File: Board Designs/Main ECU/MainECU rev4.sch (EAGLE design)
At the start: 145 parts, among them X1 CONNECTOR-37, X2 CONNECTOR-4AUTOSPORT, X3 CONNECTOR-4NANO-FIT-VERTICAL-4, X4 CONNECTOR-4NANO-FIT-VERTICAL-4

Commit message: Rename Main ECU rev1b -> rev3, rev3 -> rev4
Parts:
- removed AC1_FILTR, AC2_FILTR: 510, HyTechDevices:RESISTOR0805-RES
- removed BRAKE_LIGHT_SSR, FAN_SSR1, FAN_SSR2, INVERTER_SSR, PUMP_SSR: CPC1002N, HyTechDevices:CPC1002N
- removed BR_FILTR: 100, HyTechDevices:RESISTOR0805-RES
- removed C13: .1uF, HyTechDevices:CAP0805
- removed LED12, LED13, LED16, LED4: Red, HyTechDevices:LED-0805
- removed R25: 330, HyTechDevices:RESISTOR0805-RES
- removed REG2: 5V, HyTechDevices:OKI-78SR
- removed U$20, U$21, U$22: JUMPER, HyTechDevices:JUMPER
- added C14, C17: 47pF, HyTechDevices:CAP0805
- added C15, C16, C18, C19, C21: .1uF, HyTechDevices:CAP0805
- added C20: .22uF, HyTechDevices:CAP0805
- added CAN_TRANSCEIVER2: MCP2551, HyTechDevices:MCP2551
- added Q1, Q11, Q2, Q3, Q4, Q5, Q6, Q7, Q8, Q9: MMBT3904LT3G, HyTechDevices:BJT_NPNSOT
- added Q10: (no value), HyTechDevices:BJT_NPNSOT
- added R46: 120, HyTechDevices:RESISTOR0805-RES
- added R47, R50: 2.2k, HyTechDevices:RESISTOR0805-RES
- added R48: 10k, HyTechDevices:RESISTOR0805-RES
- added R49: 1.2k, HyTechDevices:RESISTOR0805-RES
- added REG3: 5V, HyTechDevices:OKI-78SR
- added U$27, U$28: (no value), HyTechDevices:MAX7480
- C11: value .22uF -> (none)
- C12: value 2.2µ -> .1uF
- C3: value 22µ -> 47pF
- C4: value 22µ -> .1uF
- D7, D8, D9: value DIODE0805 -> MMBZ5246BLT1G; device HyTechDevices:DIODE0805 -> HyTechDevices:DIODE_ZENER
- R10: value 43 -> 2.2k
- R16: value 43 -> 100
- R24, R27, R28: value 33 -> 10k
- R35, R36, R38, R39, R40, R41, R42: value 270 -> 2.2k
- R37: value 270 -> 0
- R44: value 0 -> 2.2k
- U$11, U$12: value TLP291-4 -> JUMPER; device HyTechDevices:TLP291-4 -> HyTechDevices:JUMPER
- U$15: value SN74LV1T34 -> BJT_PNPSOT; device HyTechDevices:SN74LV1T34 -> HyTechDevices:BJT_PNPSOT
- U$16: value JUMPER -> CR-2450/G1AN; device HyTechDevices:JUMPER -> HyTechDevices:CR-2450/G1AN
- U$19: value JUMPER -> MC34152; device HyTechDevices:JUMPER -> HyTechDevices:MC34152
- U$26: value CR-2450/G1AN -> (none); device HyTechDevices:CR-2450/G1AN -> HyTechDevices:MAX7480
- U$4, U$6, U$7: value G5LE -> N-CHANNEL_MOSFET_FQP30N06L; device HyTechDevices:G5LE -> HyTechDevices:N-CHANNEL_MOSFET_HOR_HOLE
- U$5: value CPC1002N -> MC34152; device HyTechDevices:CPC1002N -> HyTechDevices:MC34152
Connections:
- removed net DASH_CTRL5: R39.1, U$17.GPA4
- removed net DASH_CTRL6: R40.1, U$13.P$2, U$17.GPA5
- removed net DASH_CTRL7: R41.1, U$14.P$2, U$17.GPA6
- removed net DASH_CTRL8: R42.1, U$15.2, U$17.GPA7, U$19.P$2
- removed net N$20: D8.C, FAN_SSR1.DC-, U$7.COIL-
- removed net N$39: FAN_SSR2.CONTROL-, LED16.A
- removed net N$43: D10.C, R26.1, SOFTWARE_SHUTOFF.COIL-, U$5.DC-
- removed net N$44: R25.2, U$5.CONTROL-
- removed net RELAY_CTRL1: PUMP_SSR.CONTROL+, U$1.A9
- removed net RELAY_CTRL2: FAN_SSR1.CONTROL+, U$1.D2
- removed net RELAY_CTRL3: FAN_SSR2.CONTROL+, U$1.A8
- new net DASH_CTRL5_IN: U$12.P$2, U$17.GPA4
- new net DASH_CTRL5_OUT: R40.1, U$17.GPB4
- new net DASH_CTRL6_IN: U$11.P$2, U$17.GPA5
- new net DASH_CTRL6_OUT: R41.1, U$17.GPB5
- new net DASH_CTRL7_IN: U$13.P$2, U$17.GPA6
- new net DASH_CTRL7_OUT: R42.1, U$17.GPB6
- new net DASH_CTRL8_IN: U$14.P$2, U$17.GPA7
- new net DASH_CTRL8_OUT: R44.1, U$17.GPB7
- new net FAN1CONTROL: U$1.A8, U$5.IN_A
- new net FAN1DRIVE: D8.C, R24.2, U$5.OUT_A, U$7.G
- new net FAN2CONTROL: U$1.A9, U$5.IN_B
- new net FAN2DRIVE: D7.C, R28.2, U$4.G, U$5.OUT_B
- new net N$66: D4.A, Q9.COLLECTOR, U$8.COIL-
- new net PUMPCONTROL: U$1.A6, U$19.IN_A
- new net PUMPDRIVE: D9.C, R27.2, U$19.OUT_A, U$6.G
- new net TELEMETRY_CANH: CAN_TRANSCEIVER2.7, R46.2, X4-4.S
- new net TELEMETRY_CANL: CAN_TRANSCEIVER2.6, R46.1, X4-3.S
- net +12V: now also C20.2, D10.C, D4.C, R48.1, REG3.IN, SOFTWARE_SHUTOFF.COIL-, U$15.E, U$19.VCC, U$5.VCC, U$8.COIL+; no longer BRAKE_LIGHT_SSR.DC+, C11.2, FAN_SSR1.DC+, FAN_SSR2.DC+, INVERTER_SSR.DC+, PUMP_SSR.DC+, REG2.IN, U$11.C3, U$11.C4, U$12.C1, U$12.C2, U$12.C3, U$12.C4, U$16.P$1, U$21.P$1, U$5.DC+
- net +5V: now also C11.2, C15.1, C18.1, C4.1, U$26.!SHDN, U$26.VDD, U$27.!SHDN, U$27.VDD, U$28.!SHDN, U$28.VDD; no longer U$15.5, U$20.P$1, U$22.P$1
- net BRAKE_LIGHT: now also U$15.C; no longer BRAKE_LIGHT_SSR.DC-
- net CANH: no longer X4-4.S
- net CANL: no longer X4-3.S
- net DASH_CTRL1: now also U$17.GPB0; no longer U$17.GPA0
- net DASH_CTRL10: now also U$17.GPA1; no longer U$17.GPB1
- net DASH_CTRL11: now also U$17.GPA2; no longer U$17.GPB2
- net DASH_CTRL12: now also U$17.GPA3; no longer U$17.GPB3
- net DASH_CTRL2: now also U$17.GPB1; no longer U$17.GPA1
- net DASH_CTRL3: now also R38.1, U$17.GPB2; no longer R37.1, U$17.GPA2
- net DASH_CTRL4: now also R39.1, U$17.GPB3; no longer R38.1, U$17.GPA3
- net DASH_CTRL9: now also U$17.GPA0; no longer U$17.GPB0
- net DASH_IO2: now also R37.2; no longer R44.2
- net DASH_IO3: now also Q3.COLLECTOR; no longer U$12.EM2
- net DASH_IO4: now also Q4.COLLECTOR; no longer U$12.EM1
- net DASH_IO5: now also Q5.COLLECTOR, U$12.P$1; no longer U$11.EM4
- net DASH_IO6: now also Q6.COLLECTOR, U$11.P$1; no longer U$11.EM3, U$13.P$1
- net DASH_IO7: now also Q7.COLLECTOR, U$13.P$1; no longer U$11.EM2, U$14.P$1
- net DASH_IO8: now also Q8.COLLECTOR, U$14.P$1; no longer U$11.EM1, U$15.4, U$19.P$1
- net FAN1-: now also U$7.D; no longer U$7.P
- net FAN2-: now also U$4.D; no longer U$4.P
- net GND: now also C14.2, C15.2, C16.1, C17.2, C18.2, C19.1, C20.1, C21.1, CAN_TRANSCEIVER2.2, CAN_TRANSCEIVER2.8, Q1.EMITTER, Q10.EMITTER, Q11.EMITTER, Q2.EMITTER, Q3.EMITTER, Q4.EMITTER, Q5.EMITTER, Q6.EMITTER, Q7.EMITTER, Q8.EMITTER, Q9.EMITTER, R24.1, R27.1, R28.1, REG3.GND, U$19.GND, U$25.GND, U$26.GND, U$27.GND, U$28.GND, U$5.GND; no longer C13.1, D10.A, D4.A, LED4.C, R24.2, R25.1, R27.2, R28.2, REG2.GND, SOFTWARE_SHUTOFF.COIL+, U$11.GND1, U$11.GND2, U$11.GND3, U$11.GND4, U$12.GND1, U$12.GND2, U$12.GND3, U$12.GND4, U$15.3, U$4.COIL+, U$6.COIL+, U$7.COIL+, U$8.COIL-
- net INVERTER_CTRL: now also R16.1, R47.1; no longer INVERTER_SSR.CONTROL+
- net N$17: now also Q10.COLLECTOR, R48.2, R49.1; no longer BRAKE_LIGHT_SSR.CONTROL+, R10.1
- net N$21: now also C3.1, U$27.CLK; no longer D9.C, FAN_SSR2.DC-, U$4.COIL-
- net N$23: now also U$28.IN; no longer AC2_FILTR.1
- net N$24: now also U$27.IN; no longer AC1_FILTR.1
- net N$25: now also U$26.IN; no longer BR_FILTR.1
- net N$26: now also Q11.BASE, R50.2; no longer D4.C, INVERTER_SSR.DC-, U$8.COIL+
- net N$27: now also D10.A, Q11.COLLECTOR, SOFTWARE_SHUTOFF.COIL+; no longer INVERTER_SSR.CONTROL-, R16.1
- net N$30: now also Q2.BASE, R36.2; no longer LED16.C, R24.1
- net N$36: now also C16.2, U$28.COM, U$28.OS; no longer LED13.C, R28.1
- net N$37: now also C19.2, U$26.COM, U$26.OS; no longer LED12.C, R27.1
- net N$38: now also C14.1, U$28.CLK; no longer LED12.A, PUMP_SSR.CONTROL-
- net N$4: now also C12.2, U$27.COM, U$27.OS; no longer D7.C, PUMP_SSR.DC-, U$6.COIL-
- net N$41: now also C17.1, U$26.CLK; no longer U$2.3.3V_2, U$26.+
- net N$42: now also Q2.COLLECTOR, R37.1; no longer FAN_SSR1.CONTROL-, LED13.A
- net N$51: now also Q1.BASE; no longer U$12.VCC4
- net N$52: now also Q3.BASE, R38.2; no longer R36.2, U$12.VCC3
- net N$53: now also Q4.BASE, R39.2; no longer R37.2, U$12.VCC2
- net N$54: now also Q5.BASE, R40.2; no longer R38.2, U$12.VCC1
- net N$55: now also Q6.BASE, R41.2; no longer R39.2, U$11.VCC4
- net N$56: now also Q7.BASE, R42.2; no longer R40.2, U$11.VCC3
- net N$57: now also Q8.BASE, R44.2; no longer R41.2, U$11.VCC2
- net N$58: now also R49.2, U$15.B; no longer R42.2, U$11.VCC1
- net N$59: now also Q1.COLLECTOR; no longer U$12.EM4
- net N$60: now also U$16.+, U$2.3.3V_2; no longer R44.1, U$12.EM3
- net N$61: now also U$16.-, U$2.GND_2; no longer U$11.C1, U$16.P$2, U$20.P$2
- net N$62: now also CAN_TRANSCEIVER2.4, U$2.A15; no longer U$11.C2, U$21.P$2, U$22.P$2
- net N$64: now also CAN_TRANSCEIVER2.1, U$2.A14; no longer U$2.GND_2, U$26.-
- net N$65: now also Q9.BASE, R47.2; no longer U$25.GND
- net N$7: now also Q10.BASE, R10.1; no longer BRAKE_LIGHT_SSR.CONTROL-, LED4.A
- net PUMP1-: now also U$6.D; no longer U$6.P
- net READ_ACCEL1: now also U$27.OUT; no longer AC1_FILTR.2, C4.1
- net READ_ACCEL2: now also U$28.OUT; no longer AC2_FILTR.2, C3.1
- net READ_BRAKE: now also U$26.OUT; no longer BR_FILTR.2, C12.2
- net SOFTWARE_SHUTDOWN: now also R26.1, R50.1; no longer U$5.CONTROL+
- net TELEMETRY5V: now also C21.2, CAN_TRANSCEIVER2.3, REG3.OUT; no longer C13.2, REG2.OUT
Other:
- note added: "47pF for ~10Hz filter (11.3Hz)"
- note added: "Check Values, Switching V is 5V"
- note added: "Dash 5, 6, 7, 8 Can be inputs or outputs For input, solder jumper. For output, solder transistor and resistor."
- note added: "Pullup/down resistors to detect open circuit. Install only one per signal on ACCEL1 and ACCEL2."
- note removed: "Relays"
- note removed: "Use these jumpers or SN74LV1T34 only when optocoupler resistors are removed!"
- note removed: "Use these jumpers to select DASH_IO{7,8} output voltage"
- note removed: "⇩ Pullup/down resistors to detect open circuit. Install only one per signal on ACCEL1 and ACCEL2."
- moved on the sheet: 5ABOARDFUSE, 5AFUSE, 5ASHUTDOWNFUSE, ACC1_PD, ACC1_PU, ACC2_PD, ACC2_PU, ADXL345_BREAKOUT, BMS_LATCH_SSR, BMS_SSR, BOARD_TEMP, C1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

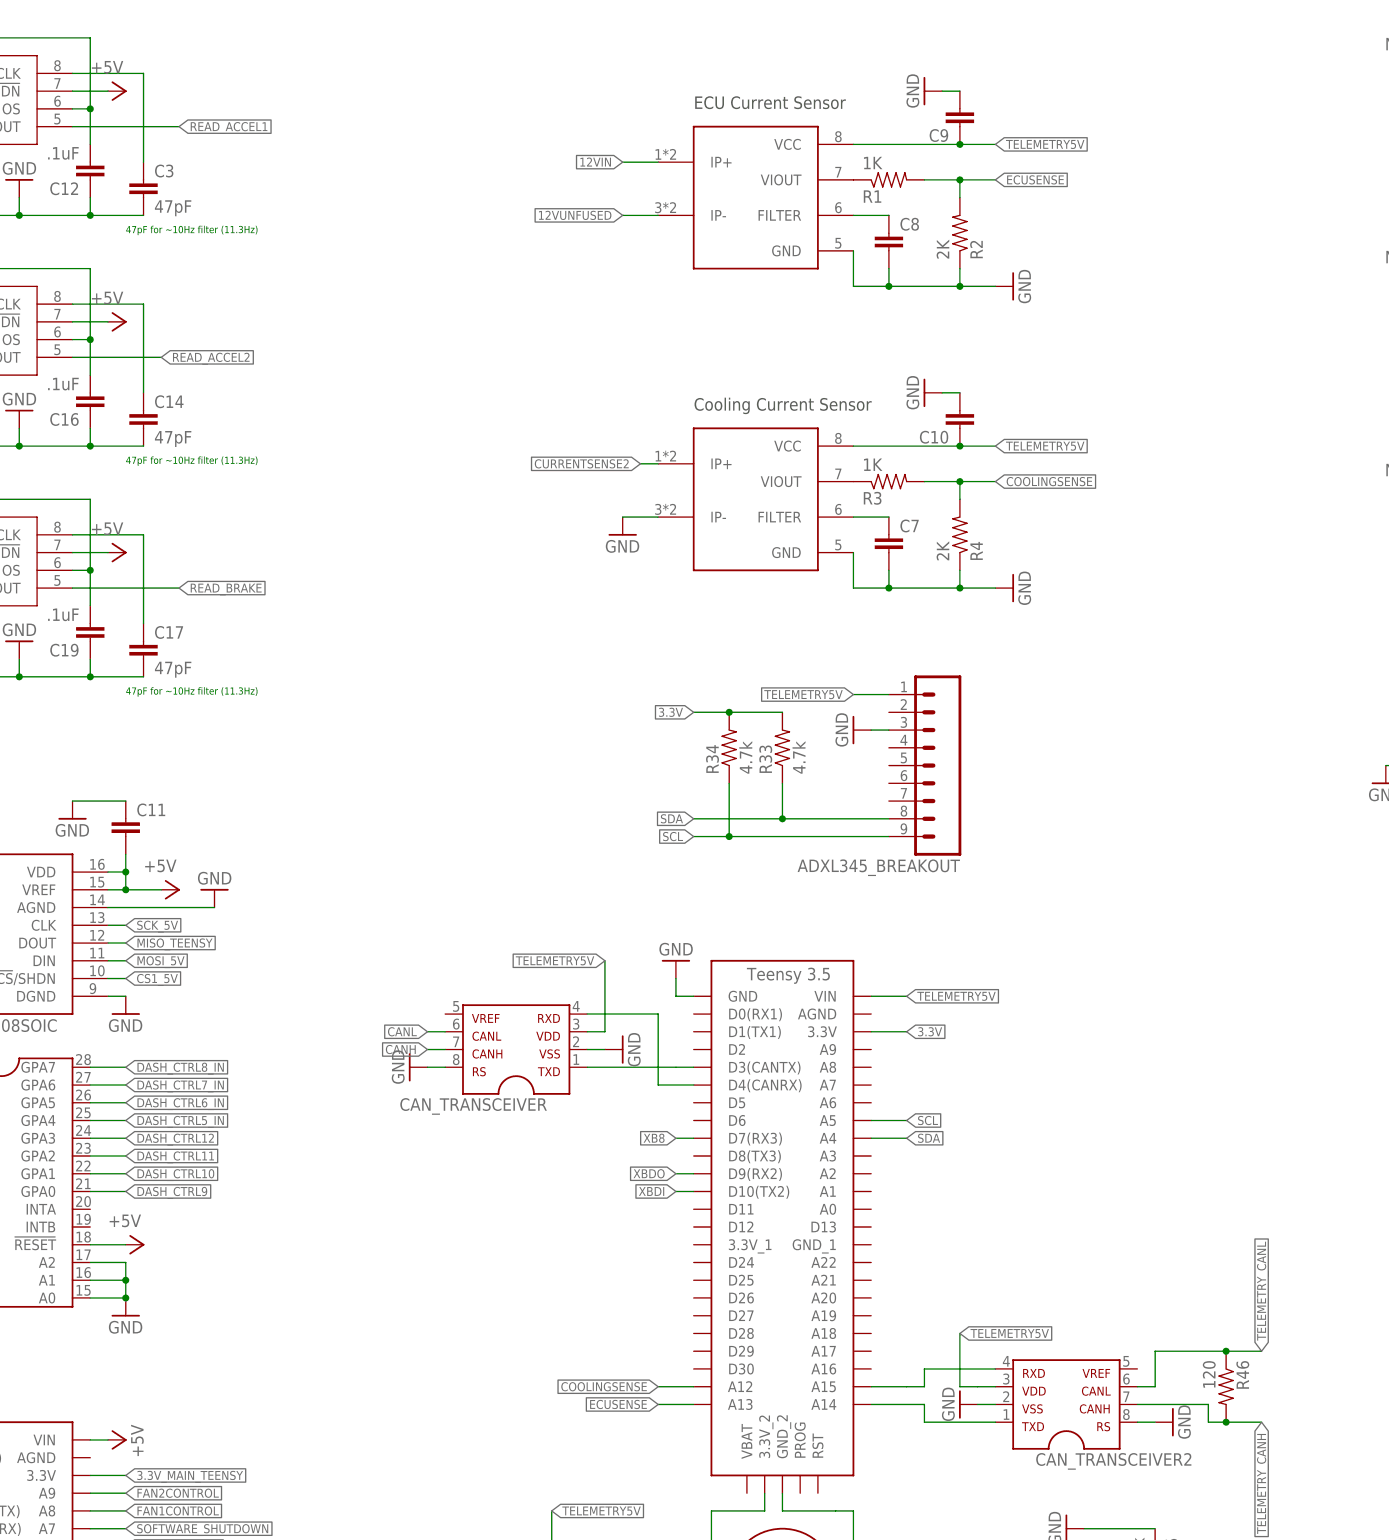
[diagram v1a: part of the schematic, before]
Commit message: Main ECU rev4: Fixed filter capacitor values again, added filters to current sensor outputs
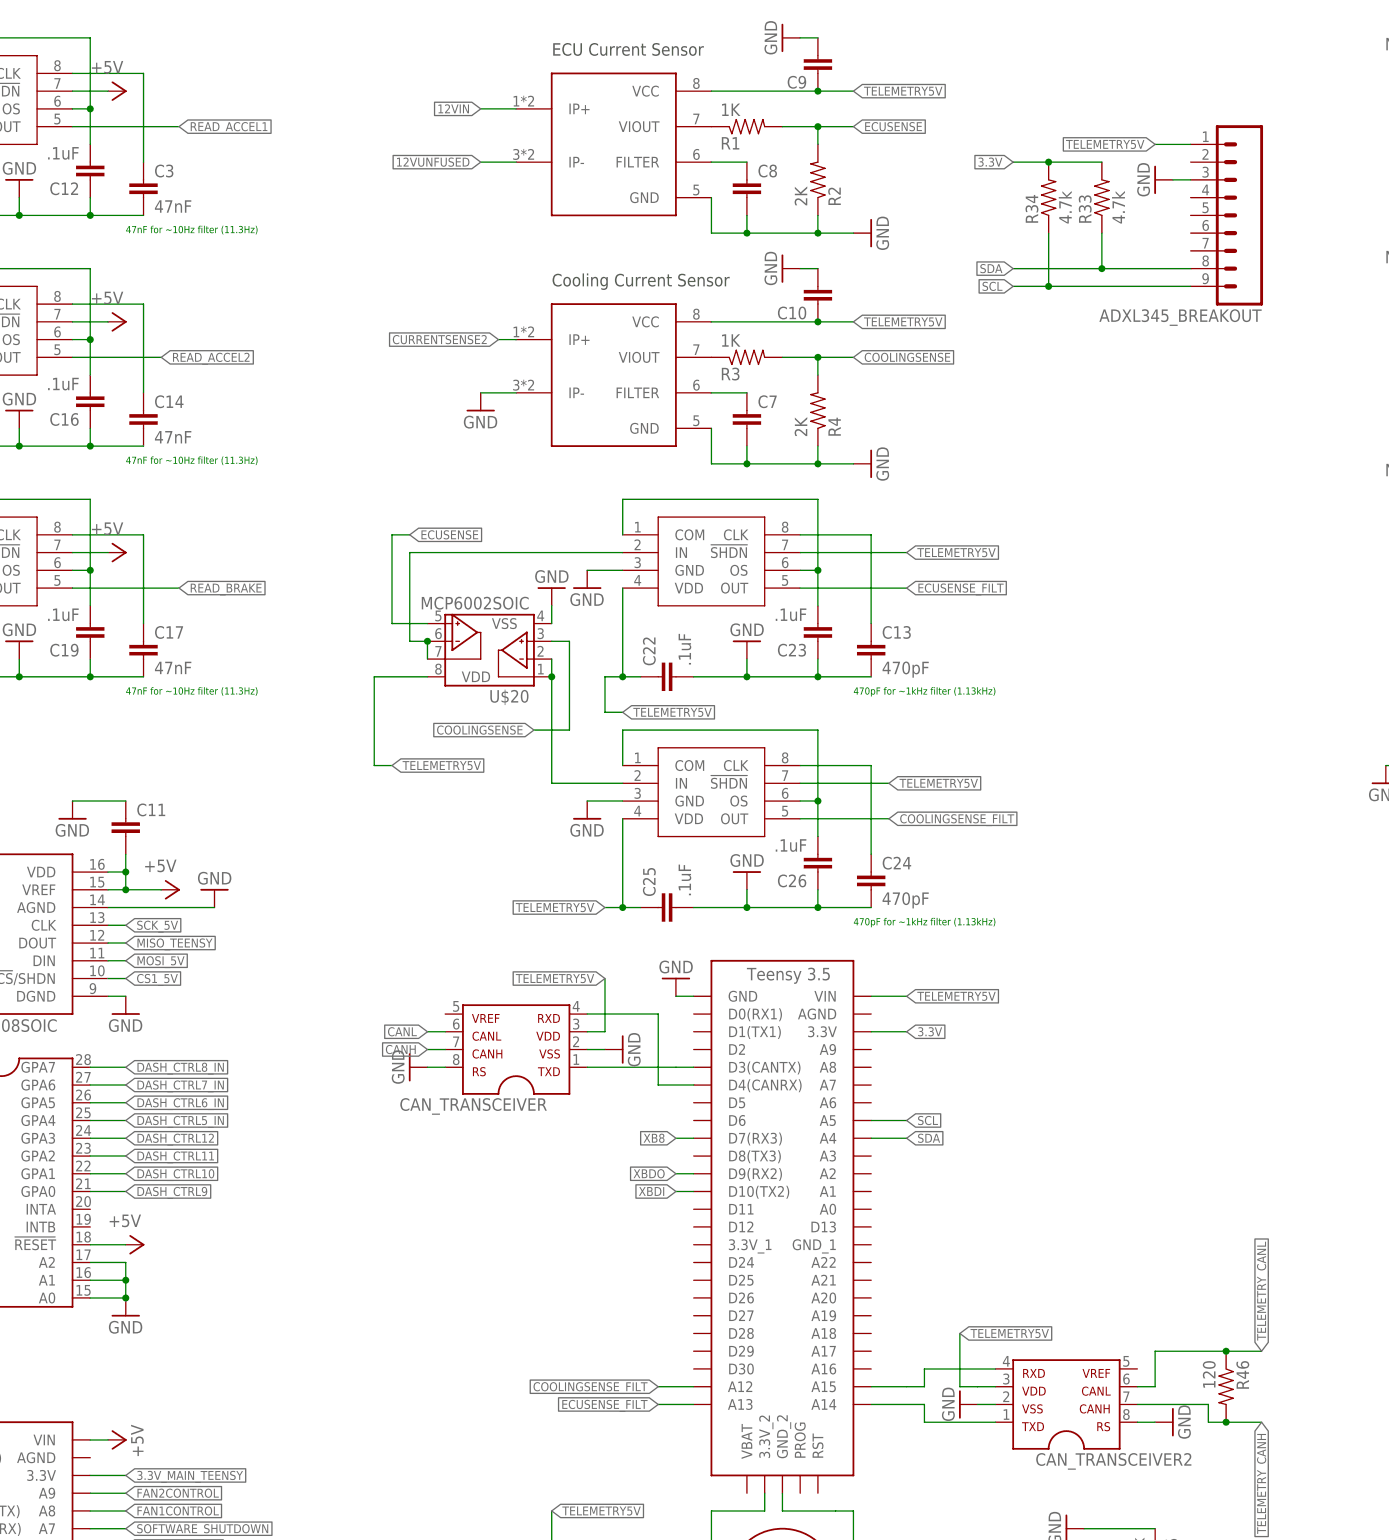
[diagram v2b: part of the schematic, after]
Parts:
- added C13, C24: 470pF, HyTechDevices:CAP0805
- added C22, C23, C25, C26: .1uF, HyTechDevices:CAP0805
- added U$20: MCP6002SOIC, HyTechDevices:MCP6002SOIC
- added U$21, U$22: (no value), HyTechDevices:MAX7480
- C14, C17, C3: value 47pF -> 47nF
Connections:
- new net COOLINGSENSE_FILT: U$2.A12, U$22.OUT
- new net ECUSENSE_FILT: U$2.A13, U$21.OUT
- new net N$20: U$20.VINA-, U$20.VOUTA, U$22.IN
- new net N$39: U$20.VINB-, U$20.VOUTB, U$21.IN
- new net N$43: C23.2, U$21.COM, U$21.OS
- new net N$44: C13.1, U$21.CLK
- new net N$67: C26.2, U$22.COM, U$22.OS
- new net N$68: C24.1, U$22.CLK
- net COOLINGSENSE: now also U$20.VINA+; no longer U$2.A12
- net ECUSENSE: now also U$20.VINB+; no longer U$2.A13
- net GND: now also C13.2, C22.2, C23.1, C24.2, C25.2, C26.1, U$20.VSS, U$21.GND, U$22.GND
- net TELEMETRY5V: now also C22.1, C25.1, U$20.VDD, U$21.!SHDN, U$21.VDD, U$22.!SHDN, U$22.VDD
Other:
- note added: "470pF for ~1kHz filter (1.13kHz)"
- note added: "47nF for ~10Hz filter (11.3Hz)"
- note removed: "47pF for ~10Hz filter (11.3Hz)"
- moved on the sheet: ADXL345_BREAKOUT, C10, C7, C8, C9, R1, R2, R3, R33, R34, R4
